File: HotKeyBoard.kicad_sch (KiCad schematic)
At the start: 218 parts, among them J1 Conn_01x12_Socket, J2 Conn_01x12_Socket, SW1 SW_Push, SW10 SW_Push, SW11 SW_Push, SW12 SW_Push, SW13 SW_Push, SW14 SW_Push, SW15 SW_Push, SW16 SW_Push, SW17 SW_Push, SW18 SW_Push, SW19 SW_Push, SW2 SW_Push, SW20 SW_Push, SW21 SW_Push, SW22 SW_Push, SW23 SW_Push, SW24 SW_Push, SW25 SW_Push, SW26 SW_Push, SW27 SW_Push, SW28 SW_Push, SW29 SW_Push, SW3 SW_Push, SW30 SW_Push, SW31 SW_Push, SW32 SW_Push, SW33 SW_Push, SW34 SW_Push, SW35 SW_Push, SW36 SW_Push, SW37 SW_Push, SW38 SW_Push, SW39 SW_Push, SW4 SW_Push, SW40 SW_Push, SW41 SW_Push, SW42 SW_Push, SW43 SW_Push, SW44 SW_Push, SW45 SW_Push, SW46 SW_Push, SW47 SW_Push, SW48 SW_Push, SW49 SW_Push, SW5 SW_Push, SW50 SW_Push, SW51 SW_Push, SW52 SW_Push, SW53 SW_Push, SW54 SW_Push, SW55 SW_Push, SW56 SW_Push, SW57 SW_Push, SW58 SW_Push, SW59 SW_Push, SW6 SW_Push, SW60 SW_Push, SW61 SW_Push, SW62 SW_Push, SW63 SW_Push, SW64 SW_Push, SW65 SW_Push, SW66 SW_Push, SW67 SW_Push, SW68 SW_Push, SW69 SW_Push, SW7 SW_Push, SW70 SW_Push, SW71 SW_Push, SW72 SW_Push, SW8 SW_Push, SW9 SW_Push

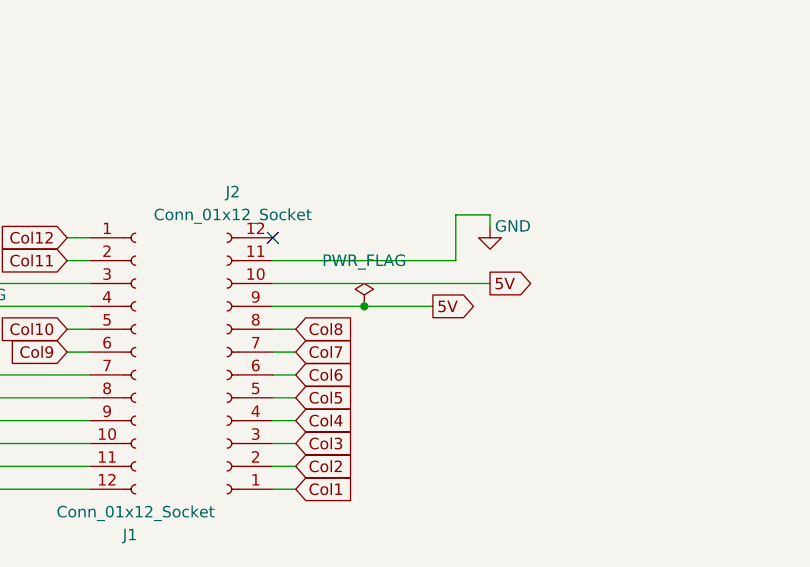
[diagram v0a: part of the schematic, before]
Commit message: Moved function key
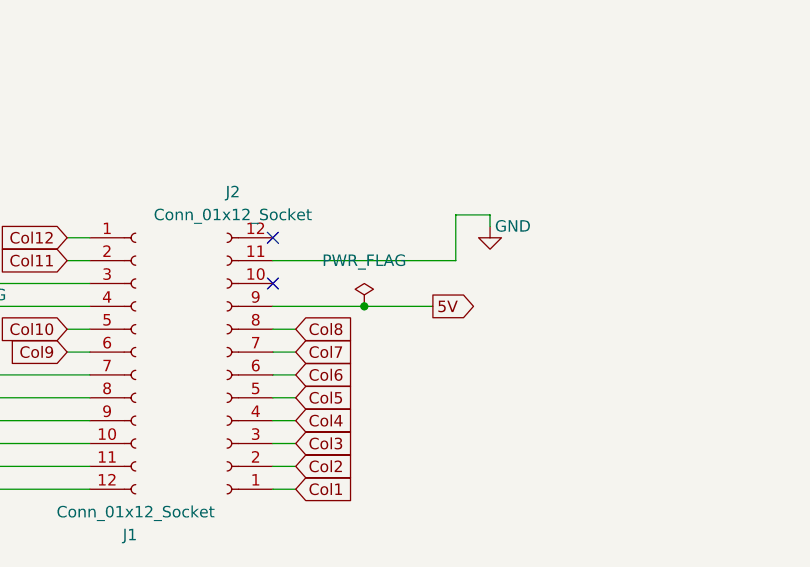
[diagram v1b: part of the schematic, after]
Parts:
- SW53, SW54, SW55, SW56: footprint Button_Switch_Keyboard:SW_Cherry_MX_1.25u_PCB -> Button_Switch_Keyboard:SW_Cherry_MX_1.00u_PCB
- SW69: footprint Button_Switch_Keyboard:SW_Cherry_MX_2.75u_PCB -> Button_Switch_Keyboard:SW_Cherry_MX_1.75u_PCB
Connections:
- net 5V: no longer J2.10 (Pin_10)
- no-connect marks 1 -> 2
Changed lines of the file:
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@@
   (junction (at 481.33 217.17) (diameter 0) (color 0 0 0 0)
   )
+  (no_connect (at 156.21 179.07))
   (no_connect (at 156.21 173.99))
   (wire (pts (xy 250.19 66.04) (xy 250.19 69.85))
@@
     (stroke (width 0) (type default))
   )
-  (wire (pts (xy 156.21 179.07) (xy 180.34 179.07))
-    (stroke (width 0) (type default))
-  )
   (wire (pts (xy 375.92 20.32) (xy 386.08 20.32))
     (stroke (width 0) (type default))
@@
     )
   )
-  (global_label "5V" (shape output) (at 180.34 179.07 0) (fields_autoplaced)
-    (effects (font (size 1.27 1.27)) (justify left))
-    (property "Intersheetrefs" "${INTERSHEET_REFS}" (at 185.6233 179.07 0)
-      (effects (font (size 1.27 1.27)) (justify left) hide)
-    )
-  )
   (global_label "Col9" (shape input) (at 292.1 294.64 270) (fields_autoplaced)
     (effects (font (size 1.27 1.27)) (justify right))
@@
       (effects (font (size 1.27 1.27)))
     )
-    (property "Footprint" "Button_Switch_Keyboard:SW_Cherry_MX_1.25u_PCB" (at 508 157.48 0)
+    (property "Footprint" "Button_Switch_Keyboard:SW_Cherry_MX_1.00u_PCB" (at 508 157.48 0)
       (effects (font (size 1.27 1.27)) hide)
     )
@@
       (effects (font (size 1.27 1.27)))
     )
-    (property "Footprint" "Button_Switch_Keyboard:SW_Cherry_MX_1.25u_PCB" (at 497.84 153.67 0)
+    (property "Footprint" "Button_Switch_Keyboard:SW_Cherry_MX_1.00u_PCB" (at 497.84 153.67 0)
       (effects (font (size 1.27 1.27)) hide)
     )
@@
       (effects (font (size 1.27 1.27)))
     )
-    (property "Footprint" "Button_Switch_Keyboard:SW_Cherry_MX_1.25u_PCB" (at 518.16 161.29 0)
+    (property "Footprint" "Button_Switch_Keyboard:SW_Cherry_MX_1.00u_PCB" (at 518.16 161.29 0)
       (effects (font (size 1.27 1.27)) hide)
     )
@@
       (effects (font (size 1.27 1.27)))
     )
-    (property "Footprint" "Button_Switch_Keyboard:SW_Cherry_MX_1.25u_PCB" (at 487.68 149.86 0)
+    (property "Footprint" "Button_Switch_Keyboard:SW_Cherry_MX_1.00u_PCB" (at 487.68 149.86 0)
       (effects (font (size 1.27 1.27)) hide)
     )
@@
       (effects (font (size 1.27 1.27)))
     )
-    (property "Footprint" "Button_Switch_Keyboard:SW_Cherry_MX_2.75u_PCB" (at 529.59 265.43 0)
+    (property "Footprint" "Button_Switch_Keyboard:SW_Cherry_MX_1.75u_PCB" (at 529.59 265.43 0)
       (effects (font (size 1.27 1.27)) hide)
     )

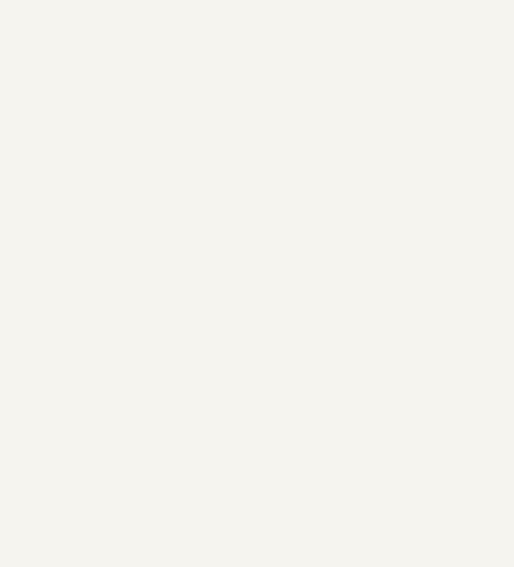
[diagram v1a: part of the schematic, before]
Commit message: Added mounting holes
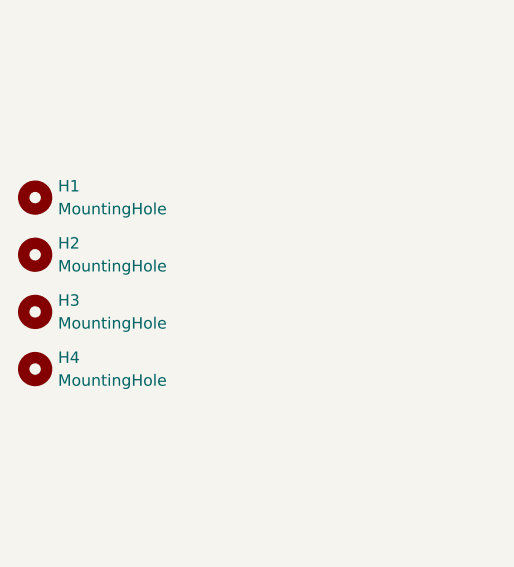
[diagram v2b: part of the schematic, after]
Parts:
- added H1, H2, H3, H4: MountingHole, MountingHole:MountingHole_3.2mm_M3_DIN965, symbol Mechanical:MountingHole
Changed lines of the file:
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@@
     )
   )
+  (symbol (lib_id "Mechanical:MountingHole") (at 92.71 60.96 0) (unit 1)
+    (in_bom yes) (on_board yes) (dnp no) (fields_autoplaced)
+    (property "Reference" "H1" (at 95.25 59.69 0)
+      (effects (font (size 1.27 1.27)) (justify left))
+    )
+    (property "Value" "MountingHole" (at 95.25 62.23 0)
+      (effects (font (size 1.27 1.27)) (justify left))
+    )
+    (property "Footprint" "MountingHole:MountingHole_3.2mm_M3_DIN965" (at 92.71 60.96 0)
+      (effects (font (size 1.27 1.27)) hide)
+    )
+    (property "Datasheet" "~" (at 92.71 60.96 0)
+      (effects (font (size 1.27 1.27)) hide)
+    )
+    (instances
+      (project "HotKeyBoard"
+        (path "/ad7237f5-a3d9-4e9d-bcab-b0d3445713fa"
+          (reference "H1") (unit 1)
+        )
+      )
+    )
+  )
   (symbol (lib_id "Switch:SW_Push") (at 528.32 170.18 0) (unit 1)
     (in_bom yes) (on_board yes) (dnp no) (fields_autoplaced)
@@
     )
   )
+  (symbol (lib_id "Mechanical:MountingHole") (at 92.71 73.66 0) (unit 1)
+    (in_bom yes) (on_board yes) (dnp no) (fields_autoplaced)
+    (property "Reference" "H3" (at 95.25 72.39 0)
+      (effects (font (size 1.27 1.27)) (justify left))
+    )
+    (property "Value" "MountingHole" (at 95.25 74.93 0)
+      (effects (font (size 1.27 1.27)) (justify left))
+    )
+    (property "Footprint" "MountingHole:MountingHole_3.2mm_M3_DIN965" (at 92.71 73.66 0)
+      (effects (font (size 1.27 1.27)) hide)
+    )
+    (property "Datasheet" "~" (at 92.71 73.66 0)
+      (effects (font (size 1.27 1.27)) hide)
+    )
+    (instances
+      (project "HotKeyBoard"
+        (path "/ad7237f5-a3d9-4e9d-bcab-b0d3445713fa"
+          (reference "H3") (unit 1)
+        )
+      )
+    )
+  )
   (symbol (lib_id "Device:D") (at 467.36 187.96 270) (unit 1)
     (in_bom yes) (on_board yes) (dnp no) (fields_autoplaced)
@@
     )
   )
+  (symbol (lib_id "Mechanical:MountingHole") (at 92.71 80.01 0) (unit 1)
+    (in_bom yes) (on_board yes) (dnp no) (fields_autoplaced)
+    (property "Reference" "H4" (at 95.25 78.74 0)
+      (effects (font (size 1.27 1.27)) (justify left))
+    )
+    (property "Value" "MountingHole" (at 95.25 81.28 0)
+      (effects (font (size 1.27 1.27)) (justify left))
+    )
+    (property "Footprint" "MountingHole:MountingHole_3.2mm_M3_DIN965" (at 92.71 80.01 0)
+      (effects (font (size 1.27 1.27)) hide)
+    )
+    (property "Datasheet" "~" (at 92.71 80.01 0)
+      (effects (font (size 1.27 1.27)) hide)
+    )
+    (instances
+      (project "HotKeyBoard"
+        (path "/ad7237f5-a3d9-4e9d-bcab-b0d3445713fa"
+          (reference "H4") (unit 1)
+        )
+      )
+    )
+  )
   (symbol (lib_id "Switch:SW_Push") (at 306.07 153.67 0) (unit 1)
     (in_bom yes) (on_board yes) (dnp no) (fields_autoplaced)
@@
         )
       )
+    )
+  )
+  (symbol (lib_id "Mechanical:MountingHole") (at 92.71 67.31 0) (unit 1)
+    (in_bom yes) (on_board yes) (dnp no) (fields_autoplaced)
+    (property "Reference" "H2" (at 95.25 66.04 0)
+      (effects (font (size 1.27 1.27)) (justify left))
+    )
+    (property "Value" "MountingHole" (at 95.25 68.58 0)
+      (effects (font (size 1.27 1.27)) (justify left))
+    )
+    (property "Footprint" "MountingHole:MountingHole_3.2mm_M3_DIN965" (at 92.71 67.31 0)
+      (effects (font (size 1.27 1.27)) hide)
+    )
+    (property "Datasheet" "~" (at 92.71 67.31 0)
+      (effects (font (size 1.27 1.27)) hide)
+    )
+    (instances
+      (project "HotKeyBoard"
+        (path "/ad7237f5-a3d9-4e9d-bcab-b0d3445713fa"
+          (reference "H2") (unit 1)
+        )
+      )

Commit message: Fixed bug in keyboard matrix
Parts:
- removed D100, D101, D102, D103, D104, D105, D106, D107, D108, D109, D110, D111, D112, D113, D114, D115, D116, D117, D118, D119, D120, D121, D122, D123, D124, D125, D126, D127, D128, D129, D130, D131, D132, D133, D134, D135, D136, D137, D138, D139, D140, D141, D142, D143, D144, D73, D74, D75, D76, D77, D78, D79, D80, D81, D82, D83, D84, D85, D86, D87, D88, D89, D90, D91, D92, D93, D94, D95, D96, D97, D98, D99: D, Diode_SMD:D_SOD-323, symbol Device:D
- SW11, SW17, SW5: footprint Button_Switch_Keyboard:SW_Cherry_MX_1.00u_PCB -> Button_Switch_Keyboard:SW_Cherry_MX_1.25u_PCB
- SW12: footprint Button_Switch_Keyboard:SW_Cherry_MX_1.00u_PCB -> Button_Switch_Keyboard:SW_Cherry_MX_2.00u_PCB
- SW2, SW24: footprint Button_Switch_Keyboard:SW_Cherry_MX_1.00u_PCB -> Button_Switch_Keyboard:SW_Cherry_MX_1.50u_PCB
- SW23, SW4: footprint Button_Switch_Keyboard:SW_Cherry_MX_1.00u_PCB -> Button_Switch_Keyboard:SW_Cherry_MX_2.25u_PCB
- SW3, SW70: footprint Button_Switch_Keyboard:SW_Cherry_MX_1.00u_PCB -> Button_Switch_Keyboard:SW_Cherry_MX_1.75u_PCB
- SW35: footprint Button_Switch_Keyboard:SW_Cherry_MX_1.00u_PCB -> Button_Switch_Keyboard:SW_Cherry_MX_6.25u_PCB
- SW49, SW50, SW51: footprint Button_Switch_Keyboard:SW_Cherry_MX_1.25u_PCB -> Button_Switch_Keyboard:SW_Cherry_MX_1.00u_PCB
- SW52: footprint Button_Switch_Keyboard:SW_Cherry_MX_6.25u_PCB -> Button_Switch_Keyboard:SW_Cherry_MX_1.00u_PCB
- SW62, SW67: footprint Button_Switch_Keyboard:SW_Cherry_MX_1.50u_PCB -> Button_Switch_Keyboard:SW_Cherry_MX_1.00u_PCB
- SW63, SW69: footprint Button_Switch_Keyboard:SW_Cherry_MX_1.75u_PCB -> Button_Switch_Keyboard:SW_Cherry_MX_1.00u_PCB
- SW64, SW68: footprint Button_Switch_Keyboard:SW_Cherry_MX_2.25u_PCB -> Button_Switch_Keyboard:SW_Cherry_MX_1.00u_PCB
- SW66: footprint Button_Switch_Keyboard:SW_Cherry_MX_2.00u_PCB -> Button_Switch_Keyboard:SW_Cherry_MX_1.00u_PCB
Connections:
- net Col12 is gone; now on net Row1: J1.1 (Pin_1)
- net Col1: now also J1.10 (Pin_10), SW10.1, SW11.1, SW12.1, SW7.1, SW8.1, SW9.1; no longer J2.1 (Pin_1)
- net Col10: now also J2.7 (Pin_7), SW61.1, SW62.1, SW63.1, SW64.1, SW65.1, SW66.1; no longer J1.5 (Pin_5)
- net Col11: now also J2.8 (Pin_8), SW67.1, SW68.1, SW69.1, SW70.1, SW71.1, SW72.1; no longer J1.2 (Pin_2)
- net Col2: now also J1.11 (Pin_11), SW13.1, SW14.1, SW15.1, SW16.1, SW17.1, SW18.1; no longer J2.2 (Pin_2)
- net Col3: now also J1.12 (Pin_12), SW19.1, SW20.1, SW21.1, SW22.1, SW23.1, SW24.1; no longer J2.3 (Pin_3)
- net Col4: now also J2.1 (Pin_1), SW25.1, SW26.1, SW27.1, SW28.1, SW29.1, SW30.1; no longer J2.4 (Pin_4)
- net Col5: now also J2.2 (Pin_2), SW31.1, SW32.1, SW33.1, SW34.1, SW35.1, SW36.1; no longer J2.5 (Pin_5)
- net Col6: now also J2.3 (Pin_3), SW37.1, SW38.1, SW39.1, SW40.1, SW41.1, SW42.1; no longer J2.6 (Pin_6)
- net Col7: now also J2.4 (Pin_4), SW43.1, SW44.1, SW45.1, SW46.1, SW47.1, SW48.1; no longer J2.7 (Pin_7)
- net Col8: now also J2.5 (Pin_5), SW49.1, SW50.1, SW51.1, SW52.1, SW53.1, SW54.1; no longer J2.8 (Pin_8)
- net Col9: now also J2.6 (Pin_6), SW55.1, SW56.1, SW57.1, SW58.1, SW59.1, SW60.1; no longer J1.6 (Pin_6)
- net GND: no longer SW1.2, SW10.2, SW11.2, SW12.2, SW13.2, SW14.2, SW15.2, SW16.2, SW17.2, SW18.2, SW19.2, SW2.2, SW20.2, SW21.2, SW22.2, SW23.2, SW24.2, SW25.2, SW26.2, SW27.2, SW28.2, SW29.2, SW3.2, SW30.2, SW31.2, SW32.2, SW33.2, SW34.2, SW35.2, SW36.2, SW37.2, SW38.2, SW39.2, SW4.2, SW40.2, SW41.2, SW42.2, SW43.2, SW44.2, SW45.2, SW46.2, SW47.2, SW48.2, SW49.2, SW5.2, SW50.2, SW51.2, SW52.2, SW53.2, SW54.2, SW55.2, SW56.2, SW57.2, SW58.2, SW59.2, SW6.2, SW60.2, SW61.2, SW62.2, SW63.2, SW64.2, SW65.2, SW66.2, SW67.2, SW68.2, SW69.2, SW7.2, SW70.2, SW71.2, SW72.2, SW8.2, SW9.2
- net Row1: now reaches D68.1 (K)
- net Row1: now also D14.1 (K), D2.1 (K), D20.1 (K), D26.1 (K), D32.1 (K), D38.1 (K), D44.1 (K), D50.1 (K), D56.1 (K), D62.1 (K), D8.1 (K); no longer SW67.1
- net Row2: now reaches D69.1 (K)
- net Row2: now also D15.1 (K), D21.1 (K), D27.1 (K), D3.1 (K), D33.1 (K), D39.1 (K), D45.1 (K), D51.1 (K), D57.1 (K), D63.1 (K), D9.1 (K), J1.5 (Pin_5); no longer SW68.1
- net Row3: now reaches D46.1 (K)
- net Row3: now also D10.1 (K), D16.1 (K), D22.1 (K), D28.1 (K), D34.1 (K), D4.1 (K), D40.1 (K), D52.1 (K), D58.1 (K), D64.1 (K), D70.1 (K), J1.6 (Pin_6); no longer SW45.1
- net Row4: now reaches D35.1 (K)
- net Row4: now also D11.1 (K), D17.1 (K), D23.1 (K), D29.1 (K), D41.1 (K), D47.1 (K), D5.1 (K), D53.1 (K), D59.1 (K), D65.1 (K), D71.1 (K), J1.7 (Pin_7); no longer SW34.1
- net Col0: now reaches SW5.1
- net Col0: now also J1.9 (Pin_9), SW1.1, SW2.1, SW3.1, SW4.1, SW6.1; no longer D5.1 (K)
- net Row5: now reaches D12.1 (K)
- net Row5: now also D18.1 (K), D24.1 (K), D30.1 (K), D36.1 (K), D42.1 (K), D48.1 (K), D54.1 (K), D6.1 (K), D60.1 (K), D66.1 (K), D72.1 (K), J1.8 (Pin_8); no longer SW12.1
- net Row0: now reaches D7.1 (K)
- net Row0: now also D1.1 (K), D13.1 (K), D19.1 (K), D25.1 (K), D31.1 (K), D37.1 (K), D43.1 (K), D49.1 (K), D55.1 (K), D61.1 (K), D67.1 (K), J1.2 (Pin_2); no longer SW7.1
- removed net Pin10: D13.2 (A), D14.2 (A), D15.2 (A), D16.2 (A), D17.2 (A), D18.2 (A), D19.2 (A), D20.2 (A), D21.2 (A), D22.2 (A), D23.2 (A), D24.2 (A), J1.10 (Pin_10)
- removed net Pin11: D49.2 (A), D50.2 (A), D51.2 (A), D52.2 (A), D53.2 (A), D54.2 (A), D55.2 (A), D56.2 (A), D57.2 (A), D58.2 (A), D59.2 (A), D60.2 (A), J1.11 (Pin_11)
- removed net Pin12: D25.2 (A), D26.2 (A), D27.2 (A), D28.2 (A), D29.2 (A), D30.2 (A), D31.2 (A), D32.2 (A), D33.2 (A), D34.2 (A), D35.2 (A), D36.2 (A), J1.12 (Pin_12)
- removed net Pin7: D61.2 (A), D62.2 (A), D63.2 (A), D64.2 (A), D65.2 (A), D66.2 (A), D67.2 (A), D68.2 (A), D69.2 (A), D70.2 (A), D71.2 (A), D72.2 (A), J1.7 (Pin_7)
- removed net Pin8: D1.2 (A), D10.2 (A), D11.2 (A), D12.2 (A), D2.2 (A), D3.2 (A), D4.2 (A), D5.2 (A), D6.2 (A), D7.2 (A), D8.2 (A), D9.2 (A), J1.8 (Pin_8)
- removed net Pin9: D37.2 (A), D38.2 (A), D39.2 (A), D40.2 (A), D41.2 (A), D42.2 (A), D43.2 (A), D44.2 (A), D45.2 (A), D46.2 (A), D47.2 (A), D48.2 (A), J1.9 (Pin_9)
- new net: D71.2 (A), SW71.2
- new net: D61.2 (A), SW61.2
- new net: D31.2 (A), SW31.2
- new net: D23.2 (A), SW23.2
- new net: D17.2 (A), SW17.2
- new net: D59.2 (A), SW59.2
- new net: D62.2 (A), SW62.2
- new net: D26.2 (A), SW26.2
- new net: D19.2 (A), SW19.2
- new net: D35.2 (A), SW35.2
- new net: D6.2 (A), SW6.2
- new net: D41.2 (A), SW41.2
- new net: D3.2 (A), SW3.2
- new net: D38.2 (A), SW38.2
- new net: D37.2 (A), SW37.2
- new net: D47.2 (A), SW47.2
- new net: D65.2 (A), SW65.2
- new net: D10.2 (A), SW10.2
- new net: D39.2 (A), SW39.2
- new net: D25.2 (A), SW25.2
- new net: D50.2 (A), SW50.2
- new net: D29.2 (A), SW29.2
- new net: D69.2 (A), SW69.2
- new net: D45.2 (A), SW45.2
- new net: D63.2 (A), SW63.2
- new net: D44.2 (A), SW44.2
- new net: D36.2 (A), SW36.2
- new net: D30.2 (A), SW30.2
- new net: D16.2 (A), SW16.2
- new net: D14.2 (A), SW14.2
- new net: D48.2 (A), SW48.2
- new net: D27.2 (A), SW27.2
- new net: D34.2 (A), SW34.2
- new net: D12.2 (A), SW12.2
- new net: D9.2 (A), SW9.2
- new net: D68.2 (A), SW68.2
- new net: D4.2 (A), SW4.2
- new net: D8.2 (A), SW8.2
- new net: D57.2 (A), SW57.2
- new net: D52.2 (A), SW52.2
- new net: D56.2 (A), SW56.2
- new net: D46.2 (A), SW46.2
- new net: D70.2 (A), SW70.2
- new net: D60.2 (A), SW60.2
- new net: D13.2 (A), SW13.2
- new net: D54.2 (A), SW54.2
- new net: D42.2 (A), SW42.2
- new net: D2.2 (A), SW2.2
- new net: D11.2 (A), SW11.2
- new net: D24.2 (A), SW24.2
- new net: D5.2 (A), SW5.2
- new net: D7.2 (A), SW7.2
- new net: D67.2 (A), SW67.2
- new net: D32.2 (A), SW32.2
- new net: D49.2 (A), SW49.2
- new net: D72.2 (A), SW72.2
- new net: D1.2 (A), SW1.2
- new net: D55.2 (A), SW55.2
- new net: D40.2 (A), SW40.2
- new net: D53.2 (A), SW53.2
- new net: D66.2 (A), SW66.2
- new net: D22.2 (A), SW22.2
- new net: D21.2 (A), SW21.2
- new net: D18.2 (A), SW18.2
- new net: D58.2 (A), SW58.2
- new net: D33.2 (A), SW33.2
- new net: D64.2 (A), SW64.2
- new net: D51.2 (A), SW51.2
- new net: D15.2 (A), SW15.2
- new net: D28.2 (A), SW28.2
- new net: D20.2 (A), SW20.2
- new net: D43.2 (A), SW43.2
